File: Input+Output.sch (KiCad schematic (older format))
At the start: 41 parts, among them J1 Switchcraft-35RAPC4BH3, J10 Switchcraft-35RAPC4BH3, J11 Switchcraft-35RAPC4BH3, J12 Switchcraft-35RAPC4BH3, J13 Conn_01x24, J14 Conn_01x24, J15 Screw_Terminal_01x03, J16 Conn_01x24, J17 Conn_01x24, J2 Switchcraft-35RAPC4BH3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

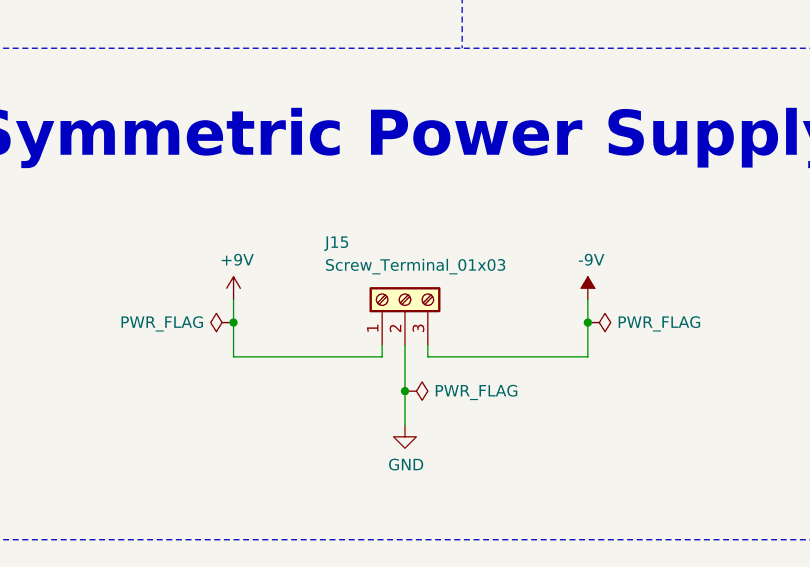
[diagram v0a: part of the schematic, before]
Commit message: added Edge.Cuts | devices arranged on PCB | added GND planes
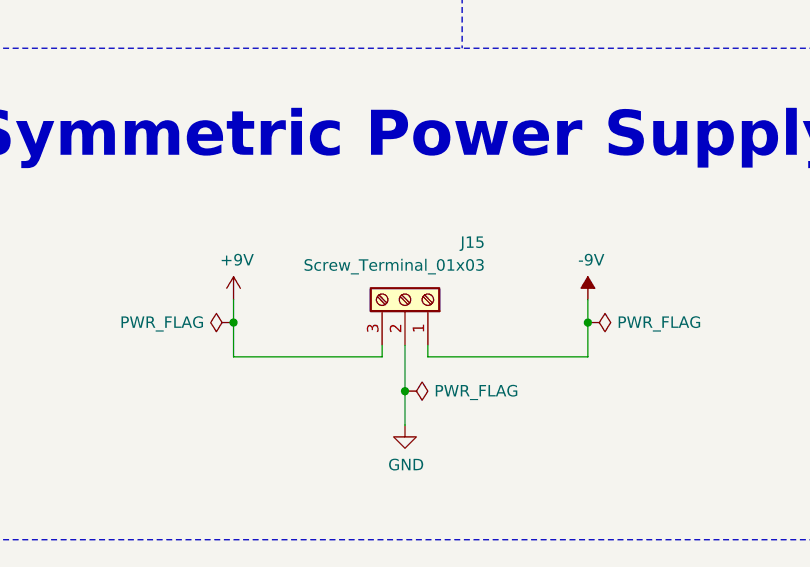
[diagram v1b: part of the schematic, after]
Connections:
- net +9V: now also J15.3 (Pin_3); no longer J15.1 (Pin_1)
- net -9V: now also J15.1 (Pin_1); no longer J15.3 (Pin_3)
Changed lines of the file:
@@
 F 3 "~" H 7800 5400 50  0001 C CNN
 	1    7800 5400
-	0    -1   -1   0
+	0    1    -1   0
 $EndComp
 $Comp

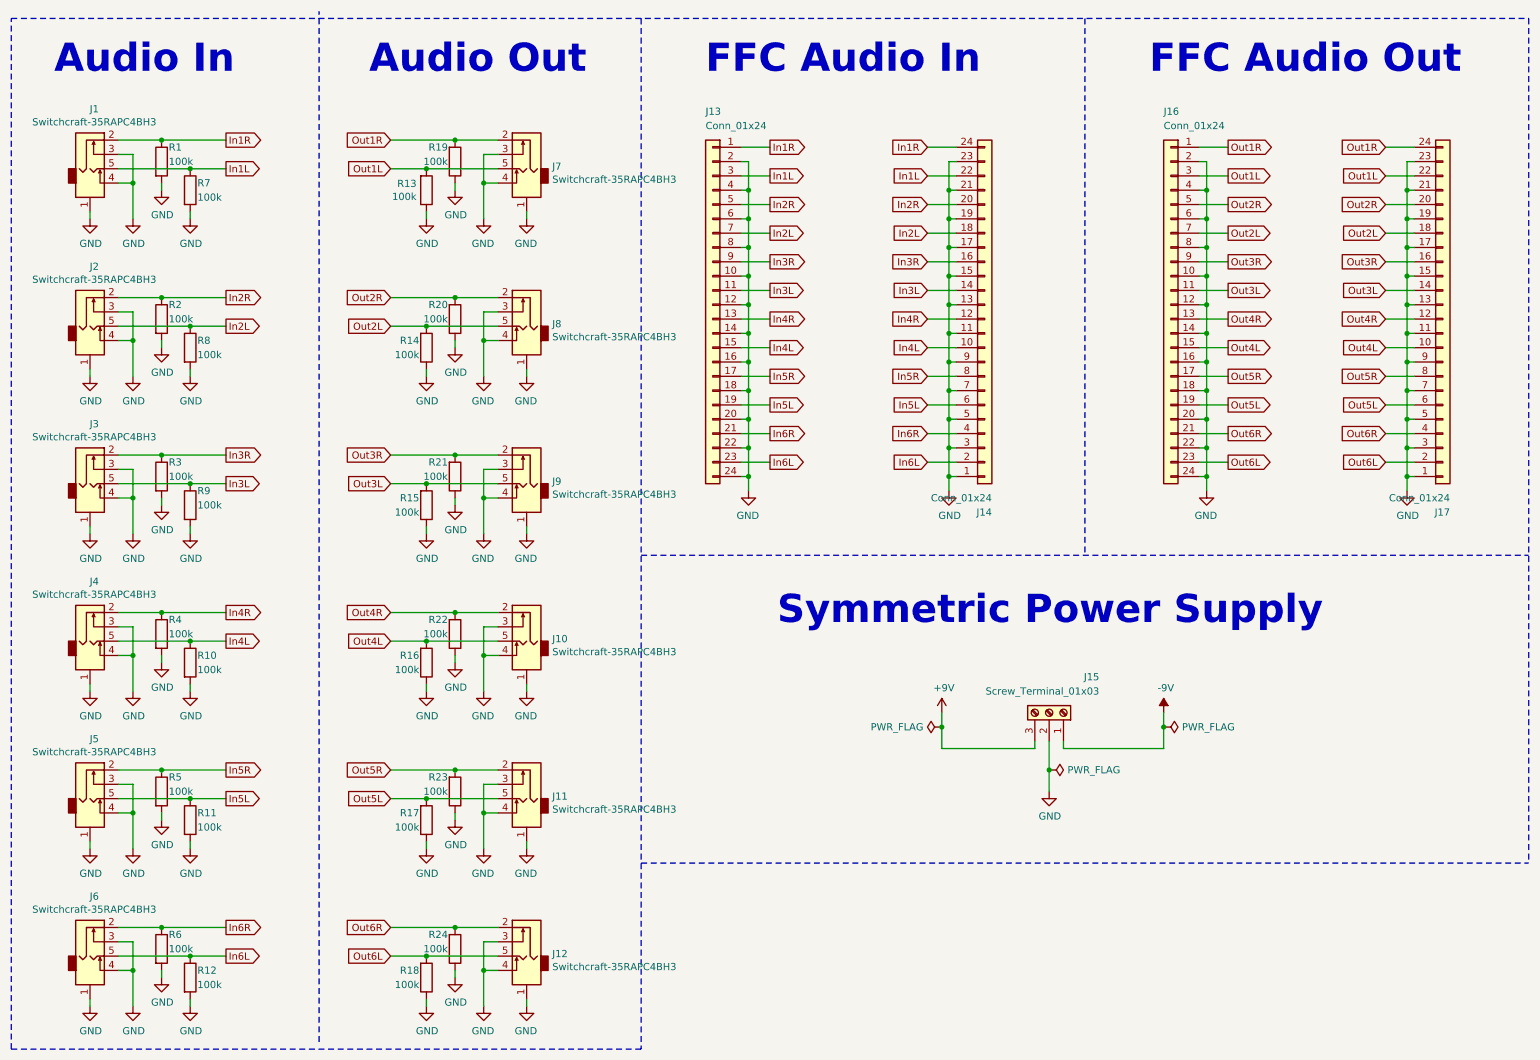
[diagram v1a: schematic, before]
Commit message: added converter for asymmetric power supply | Routing In & Out PCB finished | Routing Switch PCB started
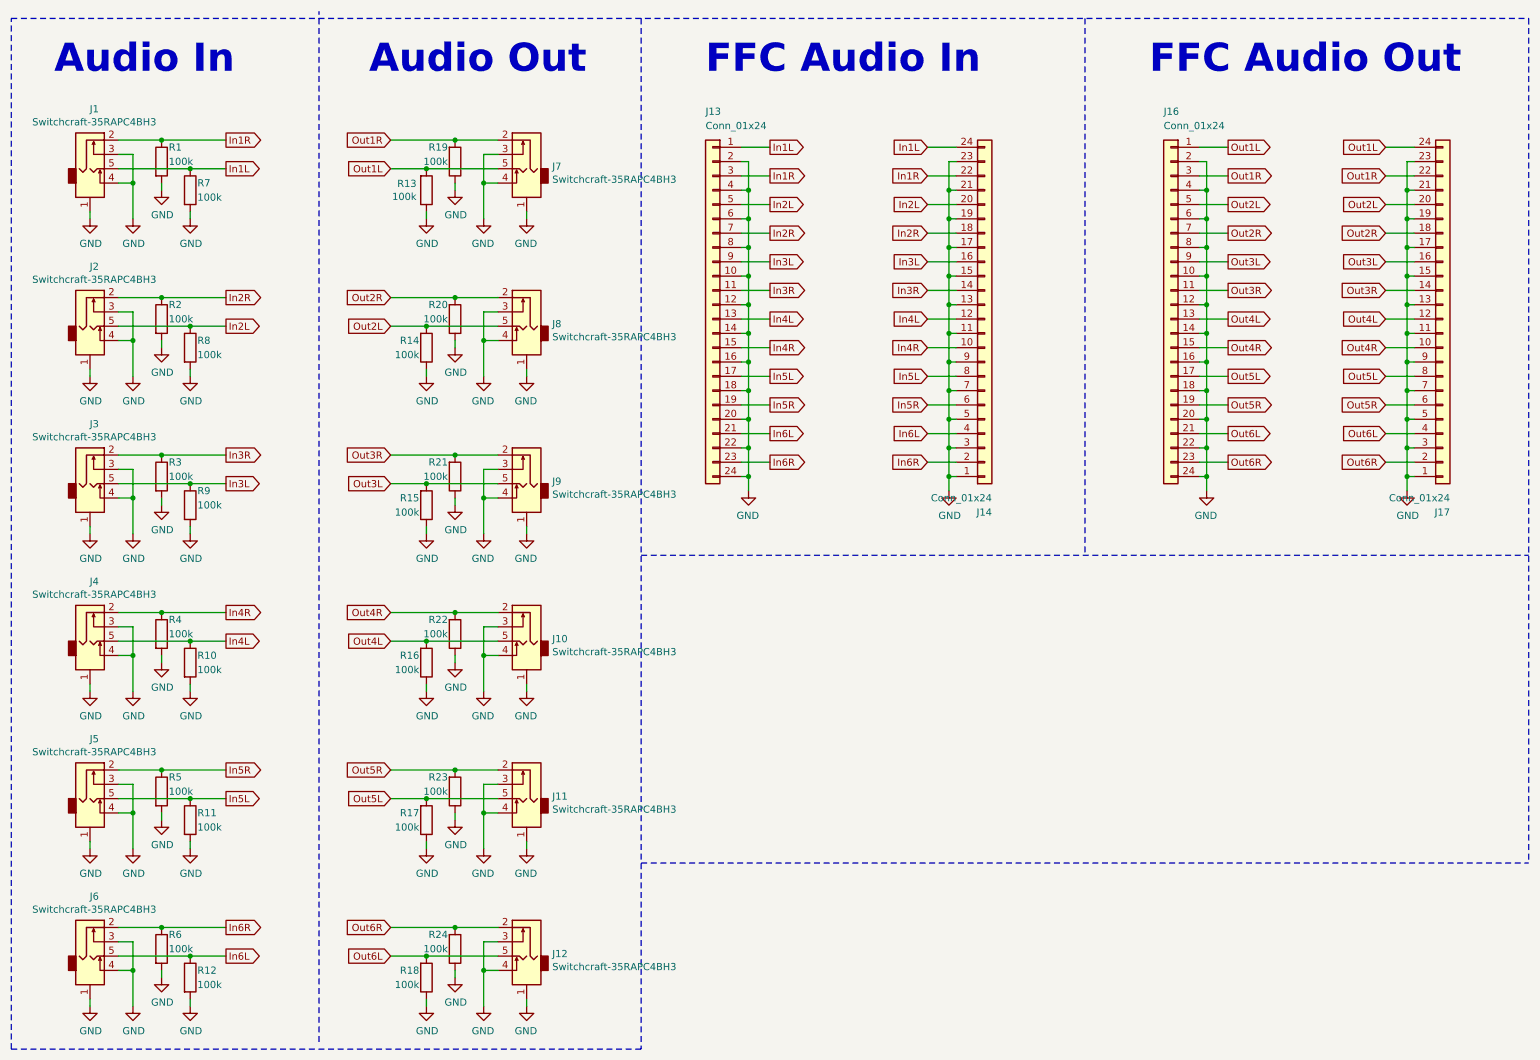
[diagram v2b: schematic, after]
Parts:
- removed J15: Screw_Terminal_01x03, h8-Connectors:Wuerth-691102710003, symbol Connector:Screw_Terminal_01x03
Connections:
- net In1L: now also J13.1 (Pin_1), J14.24 (Pin_24); no longer J13.3 (Pin_3), J14.22 (Pin_22)
- net In1R: now also J13.3 (Pin_3), J14.22 (Pin_22); no longer J13.1 (Pin_1), J14.24 (Pin_24)
- net In2L: now also J13.5 (Pin_5), J14.20 (Pin_20); no longer J13.7 (Pin_7), J14.18 (Pin_18)
- net In2R: now also J13.7 (Pin_7), J14.18 (Pin_18); no longer J13.5 (Pin_5), J14.20 (Pin_20)
- net In3L: now also J13.9 (Pin_9), J14.16 (Pin_16); no longer J13.11 (Pin_11), J14.14 (Pin_14)
- net In3R: now also J13.11 (Pin_11), J14.14 (Pin_14); no longer J13.9 (Pin_9), J14.16 (Pin_16)
- net In4L: now also J13.13 (Pin_13), J14.12 (Pin_12); no longer J13.15 (Pin_15), J14.10 (Pin_10)
- net In4R: now also J13.15 (Pin_15), J14.10 (Pin_10); no longer J13.13 (Pin_13), J14.12 (Pin_12)
- net In5L: now also J13.17 (Pin_17), J14.8 (Pin_8); no longer J13.19 (Pin_19), J14.6 (Pin_6)
- net In5R: now also J13.19 (Pin_19), J14.6 (Pin_6); no longer J13.17 (Pin_17), J14.8 (Pin_8)
- net In6L: now also J13.21 (Pin_21), J14.4 (Pin_4); no longer J13.23 (Pin_23), J14.2 (Pin_2)
- net In6R: now also J13.23 (Pin_23), J14.2 (Pin_2); no longer J13.21 (Pin_21), J14.4 (Pin_4)
- net Out1L: now also J16.1 (Pin_1), J17.24 (Pin_24); no longer J16.3 (Pin_3), J17.22 (Pin_22)
- net Out1R: now also J16.3 (Pin_3), J17.22 (Pin_22); no longer J16.1 (Pin_1), J17.24 (Pin_24)
- net Out2L: now also J16.5 (Pin_5), J17.20 (Pin_20); no longer J16.7 (Pin_7), J17.18 (Pin_18)
- net Out2R: now also J16.7 (Pin_7), J17.18 (Pin_18); no longer J16.5 (Pin_5), J17.20 (Pin_20)
- net Out3L: now also J16.9 (Pin_9), J17.16 (Pin_16); no longer J16.11 (Pin_11), J17.14 (Pin_14)
- net Out3R: now also J16.11 (Pin_11), J17.14 (Pin_14); no longer J16.9 (Pin_9), J17.16 (Pin_16)
- net Out4L: now also J16.13 (Pin_13), J17.12 (Pin_12); no longer J16.15 (Pin_15), J17.10 (Pin_10)
- net Out4R: now also J16.15 (Pin_15), J17.10 (Pin_10); no longer J16.13 (Pin_13), J17.12 (Pin_12)
- net Out5L: now also J16.17 (Pin_17), J17.8 (Pin_8); no longer J16.19 (Pin_19), J17.6 (Pin_6)
- net Out5R: now also J16.19 (Pin_19), J17.6 (Pin_6); no longer J16.17 (Pin_17), J17.8 (Pin_8)
- net Out6L: now also J16.21 (Pin_21), J17.4 (Pin_4); no longer J16.23 (Pin_23), J17.2 (Pin_2)
- net Out6R: now also J16.23 (Pin_23), J17.2 (Pin_2); no longer J16.21 (Pin_21), J17.4 (Pin_4)
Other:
- note removed: "Symmetric Power Supply"
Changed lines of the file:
@@
 Wire Wire Line
 	5650 3750 5700 3750
+Text GLabel 5850 1650 2    50   Output ~ 0
+In1R
 Text GLabel 5850 1450 2    50   Output ~ 0
-In1R
-Text GLabel 5850 1650 2    50   Output ~ 0
 In1L
+Text GLabel 5850 2050 2    50   Output ~ 0
+In2R
 Text GLabel 5850 1850 2    50   Output ~ 0
-In2R
-Text GLabel 5850 2050 2    50   Output ~ 0
 In2L
+Text GLabel 5850 2450 2    50   Output ~ 0
+In3R
 Text GLabel 5850 2250 2    50   Output ~ 0
-In3R
-Text GLabel 5850 2450 2    50   Output ~ 0
 In3L
+Text GLabel 5850 2850 2    50   Output ~ 0
+In4R
 Text GLabel 5850 2650 2    50   Output ~ 0
-In4R
-Text GLabel 5850 2850 2    50   Output ~ 0
 In4L
+Text GLabel 5850 3250 2    50   Output ~ 0
+In5R
 Text GLabel 5850 3050 2    50   Output ~ 0
-In5R
-Text GLabel 5850 3250 2    50   Output ~ 0
 In5L
+Text GLabel 5850 3650 2    50   Output ~ 0
+In6R
 Text GLabel 5850 3450 2    50   Output ~ 0
-In6R
-Text GLabel 5850 3650 2    50   Output ~ 0
 In6L
 Wire Wire Line
@@
 Wire Wire Line
 	7150 3750 7100 3750
+Text GLabel 6950 1650 0    50   Input ~ 0
+In1R
 Text GLabel 6950 1450 0    50   Input ~ 0
-In1R
-Text GLabel 6950 1650 0    50   Input ~ 0
 In1L
+Text GLabel 6950 2050 0    50   Input ~ 0
+In2R
 Text GLabel 6950 1850 0    50   Input ~ 0
-In2R
-Text GLabel 6950 2050 0    50   Input ~ 0
 In2L
+Text GLabel 6950 2450 0    50   Input ~ 0
+In3R
 Text GLabel 6950 2250 0    50   Input ~ 0
-In3R
-Text GLabel 6950 2450 0    50   Input ~ 0
 In3L
+Text GLabel 6950 2850 0    50   Input ~ 0
+In4R
 Text GLabel 6950 2650 0    50   Input ~ 0
-In4R
-Text GLabel 6950 2850 0    50   Input ~ 0
 In4L
+Text GLabel 6950 3250 0    50   Input ~ 0
+In5R
 Text GLabel 6950 3050 0    50   Input ~ 0
-In5R
-Text GLabel 6950 3250 0    50   Input ~ 0
 In5L
+Text GLabel 6950 3650 0    50   Input ~ 0
+In6R
 Text GLabel 6950 3450 0    50   Input ~ 0
-In6R
-Text GLabel 6950 3650 0    50   Input ~ 0
 In6L
 Wire Wire Line
@@
 Wire Wire Line
 	8850 3750 8900 3750
+Text GLabel 9050 1650 2    50   Output ~ 0
+Out1R
 Text GLabel 9050 1450 2    50   Output ~ 0
-Out1R
-Text GLabel 9050 1650 2    50   Output ~ 0
 Out1L
+Text GLabel 9050 2050 2    50   Output ~ 0
+Out2R
 Text GLabel 9050 1850 2    50   Output ~ 0
-Out2R
-Text GLabel 9050 2050 2    50   Output ~ 0
 Out2L
+Text GLabel 9050 2450 2    50   Output ~ 0
+Out3R
 Text GLabel 9050 2250 2    50   Output ~ 0
-Out3R
-Text GLabel 9050 2450 2    50   Output ~ 0
 Out3L
+Text GLabel 9050 2850 2    50   Output ~ 0
+Out4R
 Text GLabel 9050 2650 2    50   Output ~ 0
-Out4R
-Text GLabel 9050 2850 2    50   Output ~ 0
 Out4L
+Text GLabel 9050 3250 2    50   Output ~ 0
+Out5R
 Text GLabel 9050 3050 2    50   Output ~ 0
-Out5R
-Text GLabel 9050 3250 2    50   Output ~ 0
 Out5L
+Text GLabel 9050 3650 2    50   Output ~ 0
+Out6R
 Text GLabel 9050 3450 2    50   Output ~ 0
-Out6R
-Text GLabel 9050 3650 2    50   Output ~ 0
 Out6L
 Wire Wire Line
@@
 Wire Wire Line
 	10350 3750 10300 3750
+Text GLabel 10150 1650 0    50   Input ~ 0
+Out1R
 Text GLabel 10150 1450 0    50   Input ~ 0
-Out1R
-Text GLabel 10150 1650 0    50   Input ~ 0
 Out1L
+Text GLabel 10150 2050 0    50   Input ~ 0
+Out2R
 Text GLabel 10150 1850 0    50   Input ~ 0
-Out2R
-Text GLabel 10150 2050 0    50   Input ~ 0
 Out2L
+Text GLabel 10150 2450 0    50   Input ~ 0
+Out3R
 Text GLabel 10150 2250 0    50   Input ~ 0
-Out3R
-Text GLabel 10150 2450 0    50   Input ~ 0
 Out3L
+Text GLabel 10150 2850 0    50   Input ~ 0
+Out4R
 Text GLabel 10150 2650 0    50   Input ~ 0
-Out4R
-Text GLabel 10150 2850 0    50   Input ~ 0
 Out4L
+Text GLabel 10150 3250 0    50   Input ~ 0
+Out5R
 Text GLabel 10150 3050 0    50   Input ~ 0
-Out5R
-Text GLabel 10150 3250 0    50   Input ~ 0
 Out5L
+Text GLabel 10150 3650 0    50   Input ~ 0
+Out6R
 Text GLabel 10150 3450 0    50   Input ~ 0
-Out6R
-Text GLabel 10150 3650 0    50   Input ~ 0
 Out6L
 Wire Wire Line
@@
 	1    0    0    -1
 $EndComp
-$Comp
-L Connector:Screw_Terminal_01x03 J15
-U 1 1 5ED7C2E8
-P 7800 5400
-F 0 "J15" V 8050 5750 50  0000 R CNN
-F 1 "Screw_Terminal_01x03" V 7950 5750 50  0000 R CNN
-F 2 "h8-Connectors:Wuerth-691102710003" H 7800 5400 50  0001 C CNN
-F 3 "~" H 7800 5400 50  0001 C CNN
-	1    7800 5400
-	0    1    -1   0
-$EndComp
-$Comp
-L power:GND #PWR028
-U 1 1 5ED7CFA9
-P 7800 5950
-F 0 "#PWR028" H 7800 5700 50  0001 C CNN
-F 1 "GND" H 7805 5777 50  0000 C CNN
-F 2 "" H 7800 5950 50  0001 C CNN
-F 3 "" H 7800 5950 50  0001 C CNN
-	1    7800 5950
-	1    0    0    -1
-$EndComp
-$Comp
-L power:+9V #PWR027
-U 1 1 5ED7D07D
-P 7050 5400
-F 0 "#PWR027" H 7050 5250 50  0001 C CNN
-F 1 "+9V" H 7065 5573 50  0000 C CNN
-F 2 "" H 7050 5400 50  0001 C CNN
-F 3 "" H 7050 5400 50  0001 C CNN
-	1    7050 5400
-	1    0    0    -1
-$EndComp
-$Comp
-L power:-9V #PWR029
-U 1 1 5ED7D141
-P 8600 5400
-F 0 "#PWR029" H 8600 5275 50  0001 C CNN
-F 1 "-9V" H 8615 5573 50  0000 C CNN
-F 2 "" H 8600 5400 50  0001 C CNN
-F 3 "" H 8600 5400 50  0001 C CNN
-	1    8600 5400
-	1    0    0    -1
-$EndComp
-Wire Wire Line
-	7900 5600 7900 5650
-Wire Wire Line
-	7700 5600 7700 5650
-Wire Wire Line
-	7800 5600 7800 5800
 Text Notes 850  950  0    197  ~ 39
 Audio In
@@
 Text Notes 8500 950  0    197  ~ 39
 FFC Audio Out
-Text Notes 5900 4800 0    197  ~ 39
-Symmetric Power Supply
 Wire Notes Line width 39
 	11150 550  11150 6450
@@
 Connection ~ 3850 7200
 $Comp
-L power:PWR_FLAG #FLG0101
-U 1 1 5EF10191
-P 7050 5500
-F 0 "#FLG0101" H 7050 5575 50  0001 C CNN
-F 1 "PWR_FLAG" V 7050 5628 50  0000 L CNN
-F 2 "" H 7050 5500 50  0001 C CNN
-F 3 "~" H 7050 5500 50  0001 C CNN
-	1    7050 5500
-	0    -1   -1   0
-$EndComp
-$Comp
-L power:PWR_FLAG #FLG0102
-U 1 1 5EF101E8
-P 8600 5500
-F 0 "#FLG0102" H 8600 5575 50  0001 C CNN
-F 1 "PWR_FLAG" V 8600 5628 50  0000 L CNN
-F 2 "" H 8600 5500 50  0001 C CNN
-F 3 "~" H 8600 5500 50  0001 C CNN
-	1    8600 5500
-	0    1    1    0
-$EndComp
-$Comp
-L power:PWR_FLAG #FLG0103
-U 1 1 5EF1023F
-P 7800 5800
-F 0 "#FLG0103" H 7800 5875 50  0001 C CNN
-F 1 "PWR_FLAG" V 7800 5928 50  0000 L CNN
-F 2 "" H 7800 5800 50  0001 C CNN
-F 3 "~" H 7800 5800 50  0001 C CNN
-	1    7800 5800
-	0    1    1    0
-$EndComp
-Wire Wire Line
-	7050 5650 7050 5500
-Wire Wire Line
-	7050 5650 7700 5650
-Wire Wire Line
-	7050 5500 7050 5400
-Wire Wire Line
-	8600 5650 8600 5500
-Wire Wire Line
-	7900 5650 8600 5650
-Connection ~ 7050 5500
-Connection ~ 7800 5800
-Wire Wire Line
-	7800 5800 7800 5950
-Connection ~ 8600 5500
-Wire Wire Line
-	8600 5400 8600 5500
-$Comp
 L Device:R R1

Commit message: finished routing | added GND polygon | added description in surface plot  | added pictures to README.md documentation | changed LICENCE.md to CC BY 4.0
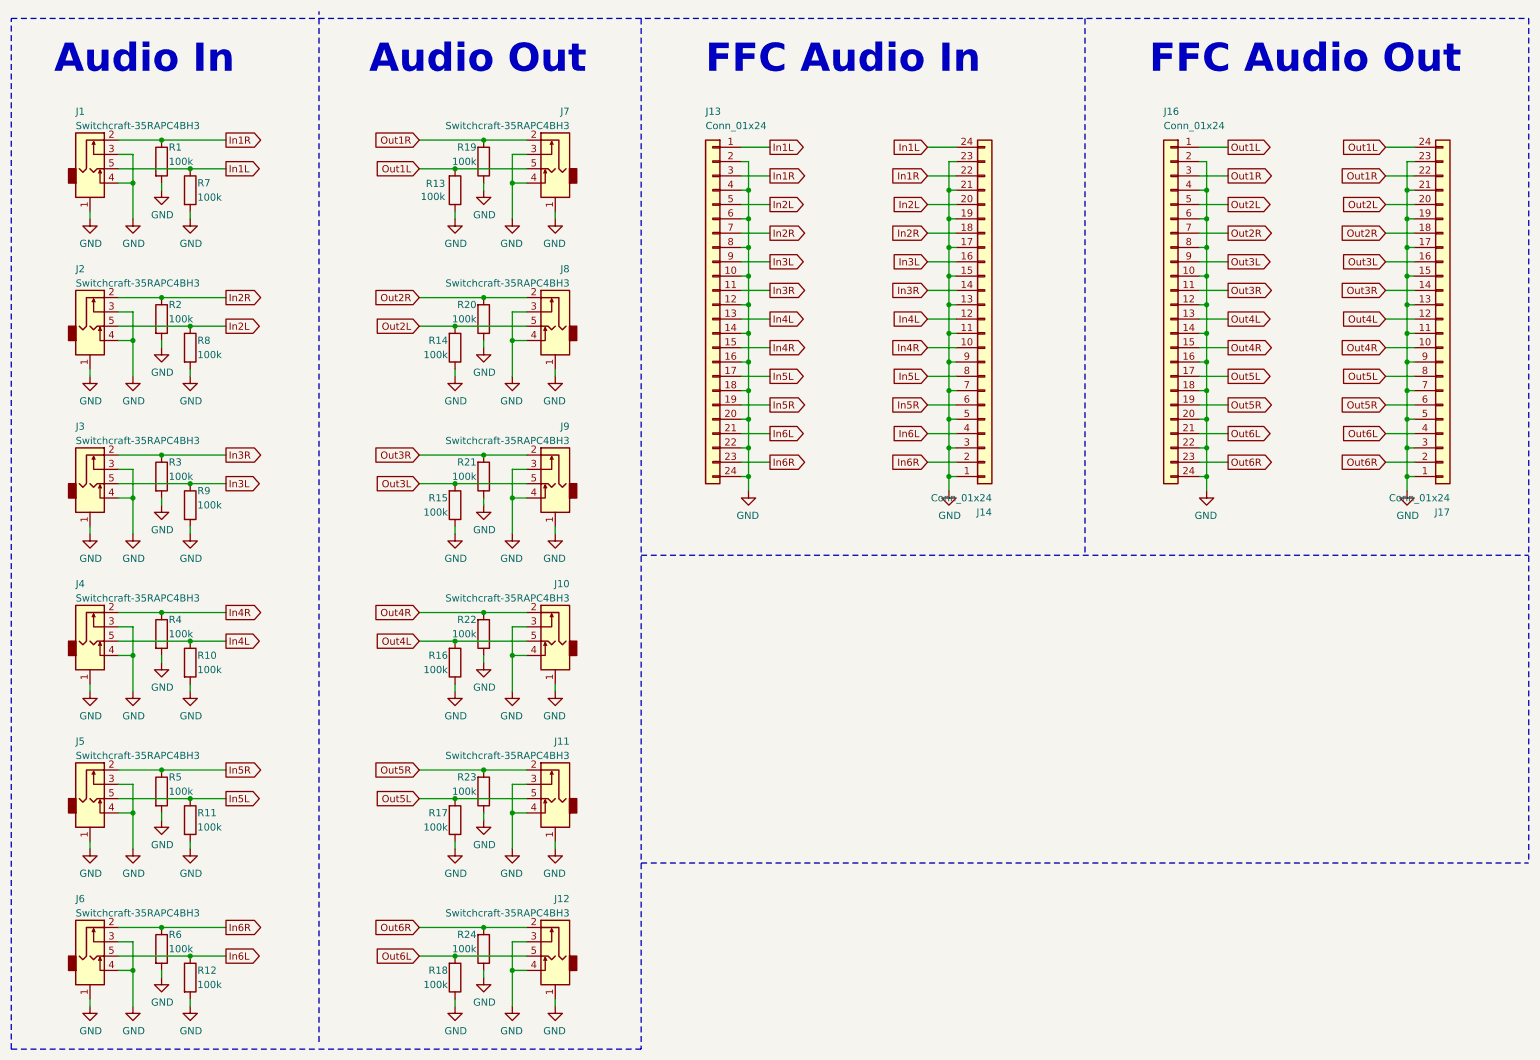
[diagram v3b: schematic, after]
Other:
- moved on the sheet: J10, J11, J12, J7, J8, J9, R13, R14, R15, R16, R17, R18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

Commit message: added new attributes MF, MFN, Mouser, Digi-Key, RS-Online, Infopage, datasheet | bill of material (BOM) created | infobox updated | added AudioBürokrat logo on silkscreen
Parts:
- J1, J10, J11, J12, J2, J3, J4, J5, J6, J7, J8, J9: Digi-Key (none) -> SC1464-ND; Infopage (none) -> http://www.switchcraft.com/ProductSummary.aspx?Parent=425; MF (none) -> Switchcraft; MFN (none) -> 35RAPC4BH3; Mouser (none) -> 502-35RAPC4BH3; RS-Online (none) -> 35RAPC4BH3
- J13, J14, J16, J17: Digi-Key (none) -> 732-686124188622CT-ND; Infopage (none) -> https://www.we-online.com/catalog/en/FPC_1_00_SMT_LIF_HORIZ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; MF (none) -> Wuerth; MFN (none) -> 686124188622; Mouser (none) -> 710-686124188622; RS-Online (none) -> —
- R1, R10, R11, R12, R13, R14, R15, R16, R17, R18, R19, R2, R20, R21, R22, R23, R24, R3, R4, R5, R6, R7, R8, R9: Digi-Key (none) -> 541-3950-1-ND; Infopage (none) -> —; MF (none) -> Vishay; MFN (none) -> CRCW0603100KFKEAC; Mouser (none) -> 71-CRCW0603100KFKEAC; RS-Online (none) -> 820-6745
